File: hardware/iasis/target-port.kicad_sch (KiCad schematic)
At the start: 0 parts

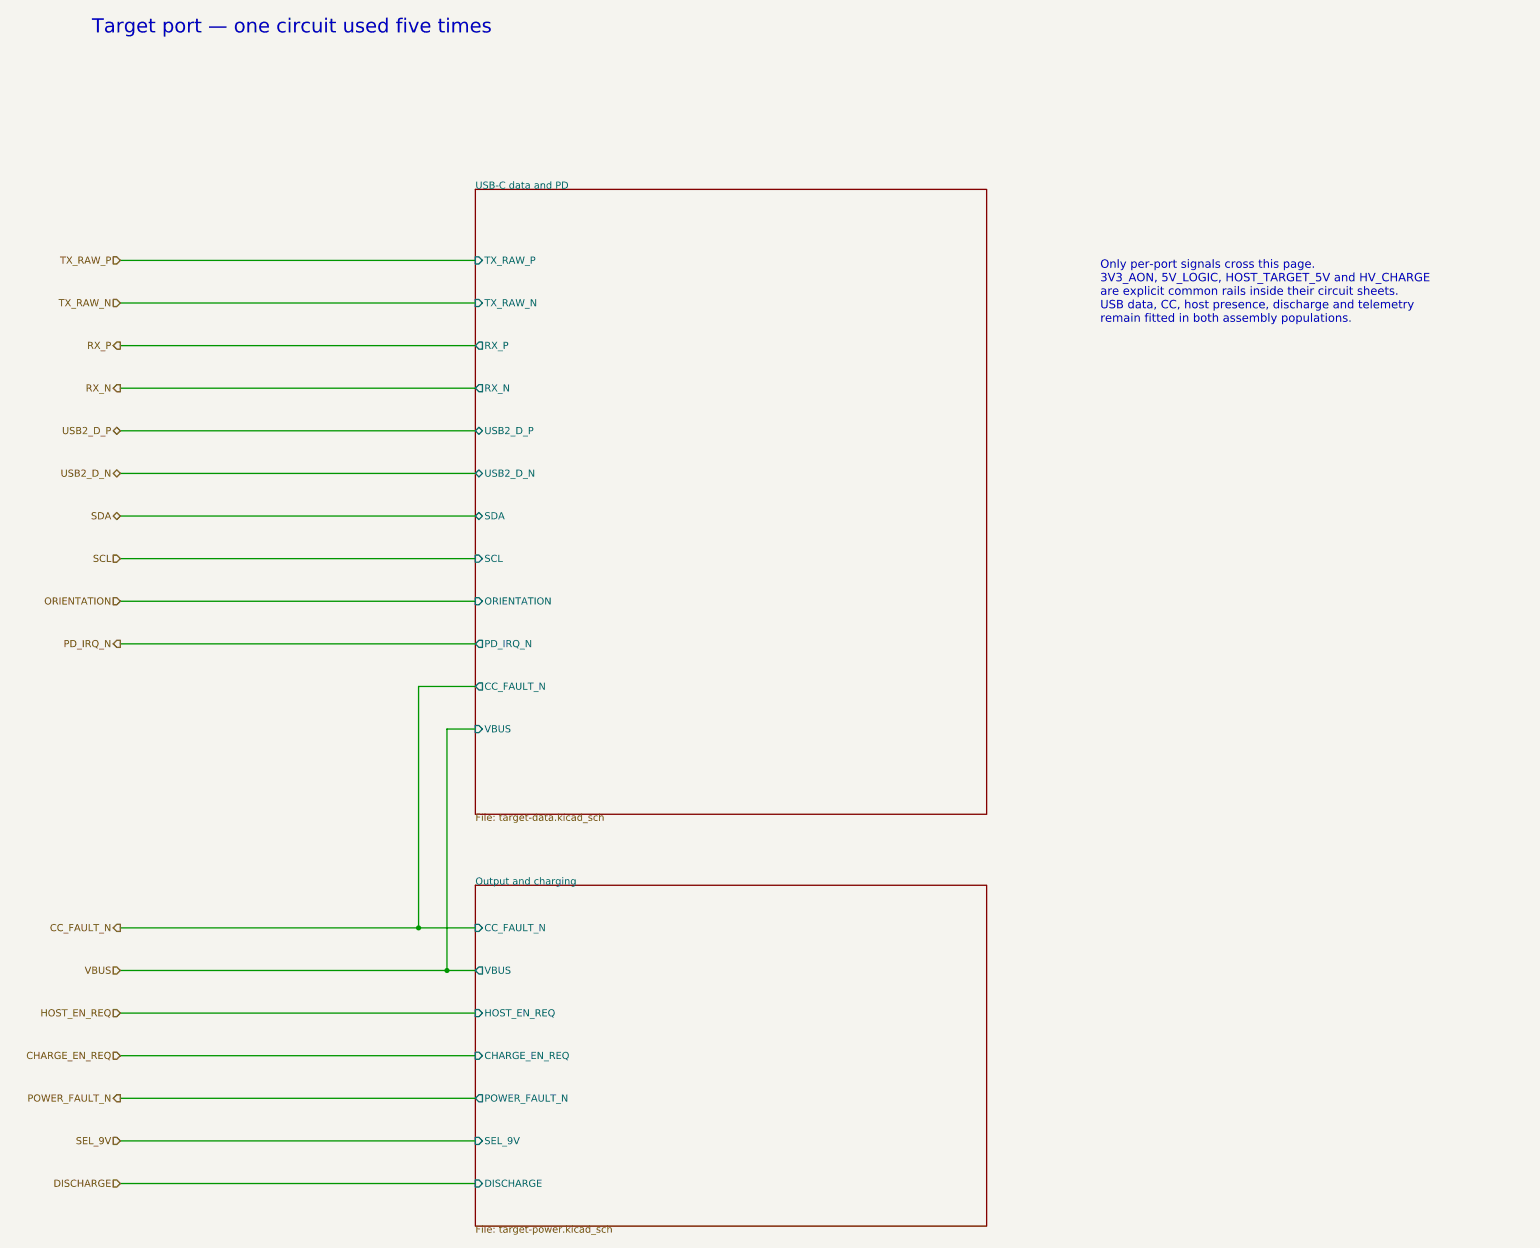
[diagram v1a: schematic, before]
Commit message: Redraw the target port sheets
The per-port data, output and charging sheets follow the signal and
power paths left to right. The receptacle sits at the right edge with
its CC and USB 2 protection wired to it, the SuperSpeed mux and ESD
arrays below, and the charging buck, feedback divider, OVP network and
output eFuse in one row. The port sheet joins its two blocks with
wires. The netlist is unchanged.
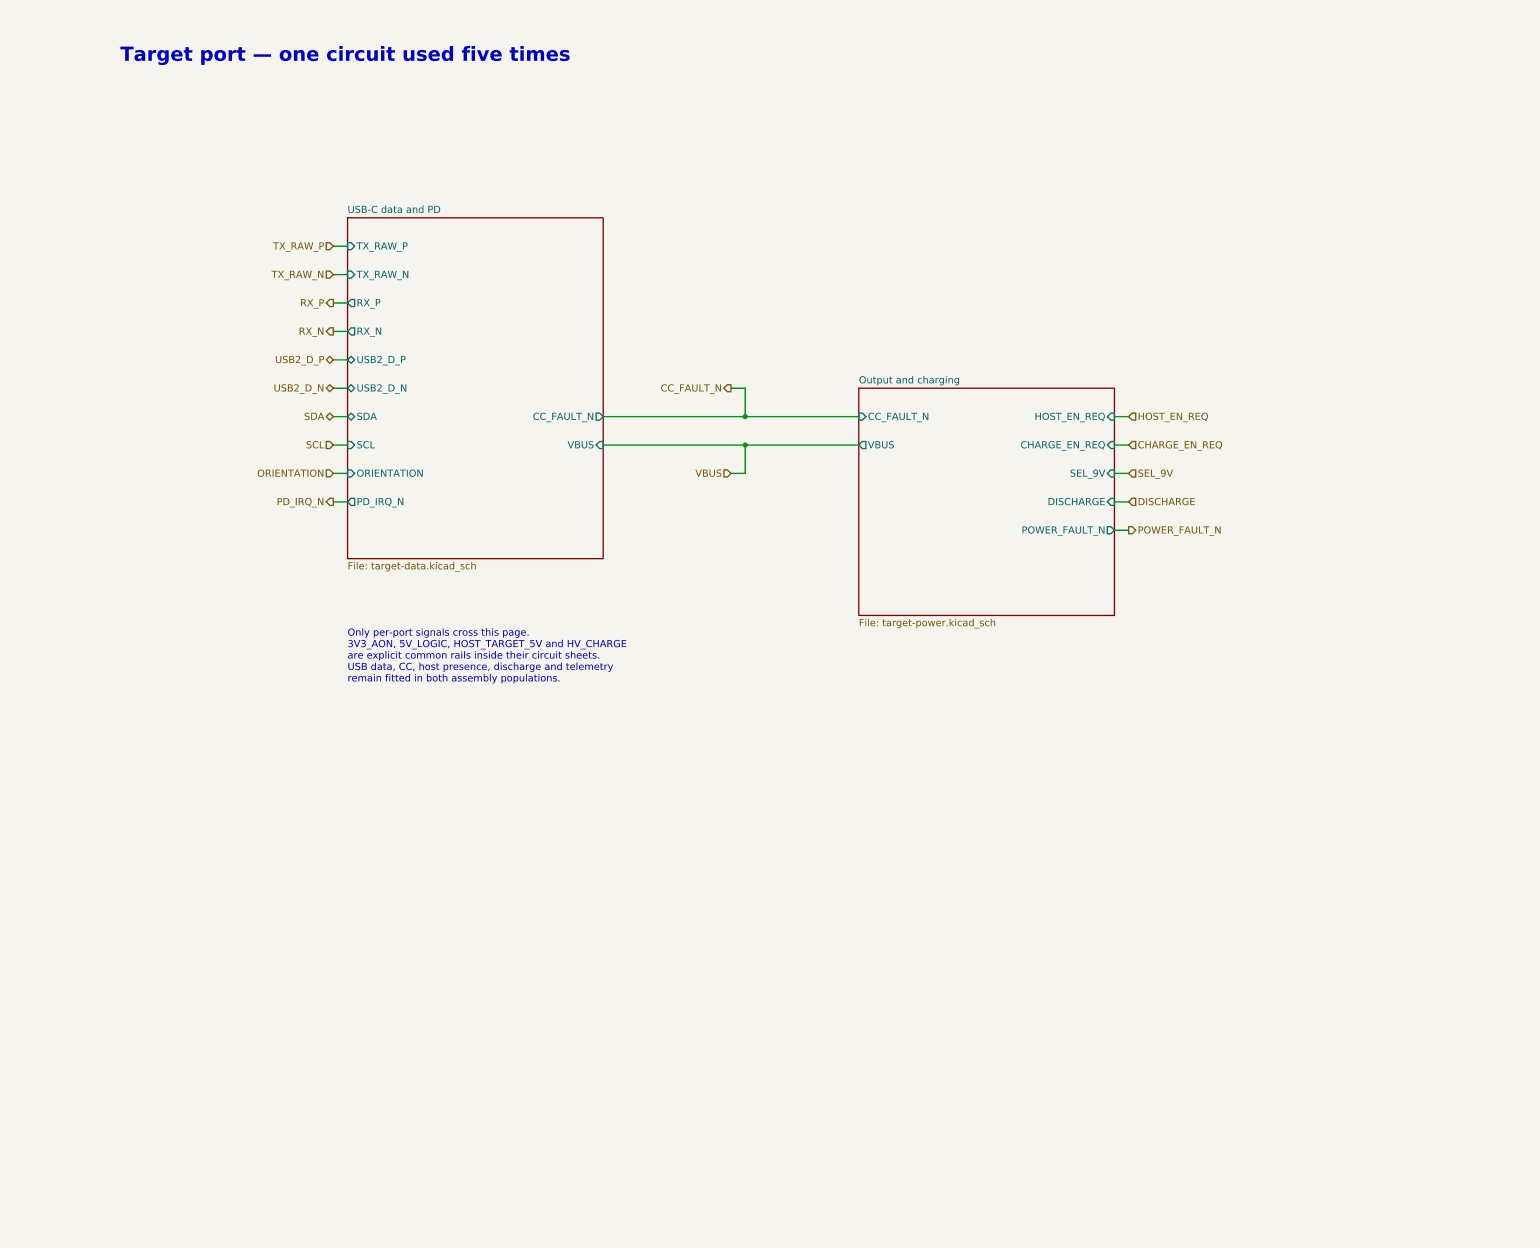
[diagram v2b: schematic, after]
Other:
- title: (none) -> Target port — one circuit used five times
